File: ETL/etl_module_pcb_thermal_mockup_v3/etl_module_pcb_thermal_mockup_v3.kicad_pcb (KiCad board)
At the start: 4 copper layers, 44.1 x 57.5 mm, 23 parts, among them J3 Conn_02x05_Counter_Clockwise, U1 ETROC_dummy_thermal_sensors, U2 ETROC_dummy_thermal_sensors, U3 ETROC_dummy_thermal_sensors, U4 ETROC_dummy_thermal_sensors, U5 ADC088SO22, U6 ADC088SO22, U7 ADC088SO22, U8 ADC088SO22

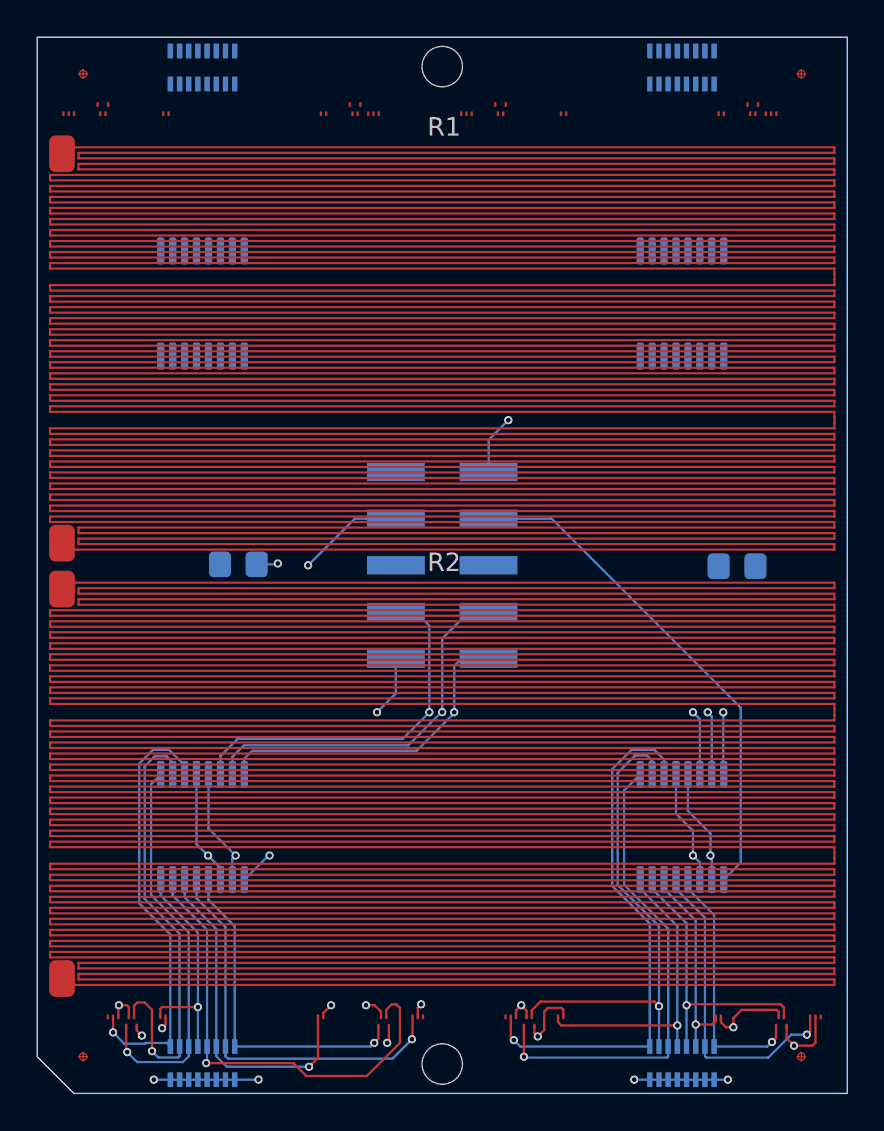
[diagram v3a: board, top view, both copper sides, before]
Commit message: Finishes redesigned draft of etl_module_pcb_thermal_mockup_v3
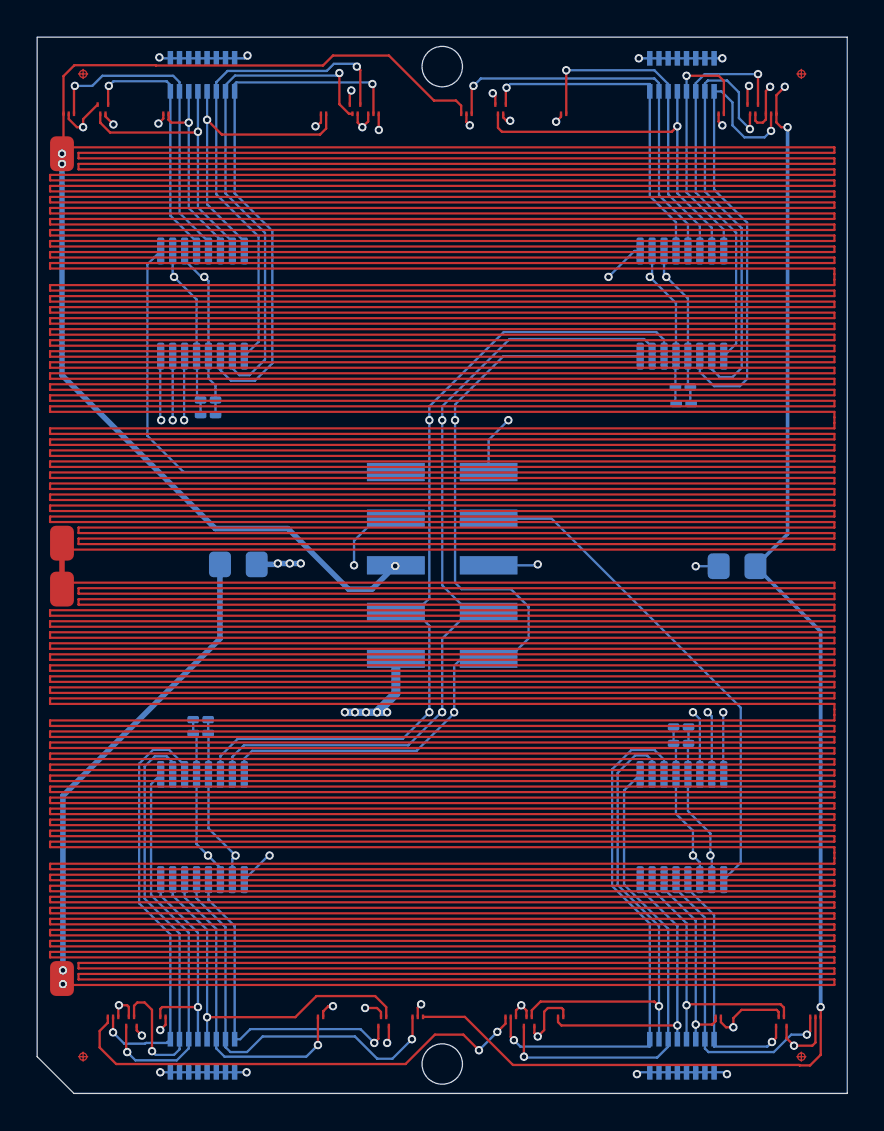
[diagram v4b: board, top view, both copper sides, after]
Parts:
- added C1: 1.0uF, Capacitor_SMD:C_0201_0603Metric_Pad0.64x0.40mm_HandSolder, B.Cu at (8.90, 37.1)
- added C2: 0.1uF, Capacitor_SMD:C_0201_0603Metric_Pad0.64x0.40mm_HandSolder, B.Cu at (8.90, 37.9)
- added C3: 1.0uF, Capacitor_SMD:C_0201_0603Metric_Pad0.64x0.40mm_HandSolder, B.Cu at (35.0, 37.5)
- added C4: 0.1uF, Capacitor_SMD:C_0201_0603Metric_Pad0.64x0.40mm_HandSolder, B.Cu at (35.0, 38.5)
- added C5: 1.0uF, Capacitor_SMD:C_0201_0603Metric_Pad0.64x0.40mm_HandSolder, B.Cu at (9.30, 20.6)
- added C6: 0.1uF, Capacitor_SMD:C_0201_0603Metric_Pad0.64x0.40mm_HandSolder, B.Cu at (9.30, 19.8)
- added C7: 1.0uF, Capacitor_SMD:C_0201_0603Metric_Pad0.64x0.40mm_HandSolder, B.Cu at (35.2, 19.9)
- added C8: 0.1uF, Capacitor_SMD:C_0201_0603Metric_Pad0.64x0.40mm_HandSolder, B.Cu at (35.1, 19.1)
- moved RN3 0.40 mm to (9.00, 2.05)
- moved RN4 0.40 mm to (35.1, 2.05)
- moved RN1 0.40 mm to (9.00, 55.5)
- moved RN2 0.40 mm to (35.1, 55.5)
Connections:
- R1 pad 1: Net-(R1-Pad1) -> VCC
- R1 pad 2: VCC -> Net-(R1-Pad2)
- R2 pad 1: Net-(JMPR1-Pad1) -> Net-(R1-Pad2)
- R2 pad 2: Net-(R1-Pad1) -> Net-(JMPR1-Pad1)
- RN3 pad 10: /X3EBR -> Net-(RN3-Pad10)
- RN3 pad 11: /X3LTR -> Net-(RN3-Pad11)
- RN3 pad 12: /X3ETR -> Net-(RN3-Pad12)
- RN3 pad 13: /X3LTL -> Net-(RN3-Pad13)
- RN3 pad 14: /X3ETL -> Net-(U3-Pad81)
- RN3 pad 15: /X3LBL -> Net-(U3-Pad117)
- RN3 pad 16: /X3EBL -> Net-(RN3-Pad16)
- RN3 pad 9: /X3LBR -> Net-(RN3-Pad9)
- RN4 pad 10: /X4EBR -> Net-(RN4-Pad10)
- RN4 pad 11: /X4LTR -> Net-(RN4-Pad11)
- RN4 pad 12: /X4ETR -> Net-(RN4-Pad12)
- RN4 pad 13: /X4LTL -> Net-(RN4-Pad13)
- RN4 pad 14: /X4ETL -> Net-(RN4-Pad14)
- RN4 pad 15: /X4LBL -> Net-(RN4-Pad15)
- RN4 pad 16: /X4EBL -> Net-(RN4-Pad16)
- RN4 pad 9: /X4LBR -> Net-(RN4-Pad9)
- U3 pad 1: VCC -> /VSS
- U3 pad 104: /X3LBR -> Net-(RN3-Pad16)
- U3 pad 107: /X3ETR -> Net-(RN3-Pad13)
- U3 pad 11: /X3LBL -> Net-(RN3-Pad10)
- U3 pad 117: /X3EBR -> Net-(U3-Pad117)
- U3 pad 121: /VSS -> VCC
- U3 pad 21: /X3LTL -> Net-(RN3-Pad12)
- U3 pad 3: /X3EBL -> Net-(RN3-Pad9)
- U3 pad 8: /X3ETL -> Net-(RN3-Pad11)
- U3 pad 81: /X3LTR -> Net-(U3-Pad81)
- U4 pad 1: VCC -> /VSS
- U4 pad 104: /X4LBR -> Net-(RN4-Pad16)
- U4 pad 107: /X4ETR -> Net-(RN4-Pad13)
- U4 pad 11: /X4LBL -> Net-(RN4-Pad10)
- U4 pad 117: /X4EBR -> Net-(RN4-Pad15)
- U4 pad 121: /VSS -> VCC
- U4 pad 21: /X4LTL -> Net-(RN4-Pad12)
- U4 pad 3: /X4EBL -> Net-(RN4-Pad9)
- U4 pad 8: /X4ETL -> Net-(RN4-Pad11)
- U4 pad 81: /X4LTR -> Net-(RN4-Pad14)
- U7 pad 10: /X3EBR -> Net-(RN3-Pad10)
- U7 pad 11: /X3LBR -> Net-(RN3-Pad9)
- U7 pad 4: /X3EBL -> Net-(RN3-Pad16)
- U7 pad 5: /X3LBL -> Net-(U3-Pad117)
- U7 pad 6: /X3ETL -> Net-(U3-Pad81)
- U7 pad 7: /X3LTL -> Net-(RN3-Pad13)
- U7 pad 8: /X3ETR -> Net-(RN3-Pad12)
- U7 pad 9: /X3LTR -> Net-(RN3-Pad11)
- U8 pad 10: /X4EBR -> Net-(RN4-Pad10)
- U8 pad 11: /X4LBR -> Net-(RN4-Pad9)
- U8 pad 4: /X4EBL -> Net-(RN4-Pad16)
- U8 pad 5: /X4LBL -> Net-(RN4-Pad15)
- U8 pad 6: /X4ETL -> Net-(RN4-Pad14)
- U8 pad 7: /X4LTL -> Net-(RN4-Pad13)
- U8 pad 8: /X4ETR -> Net-(RN4-Pad12)
- U8 pad 9: /X4LTR -> Net-(RN4-Pad11)
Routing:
- net VCC: track 0.00 -> 118.1 mm, vias 0 -> 5
- net /VSS: track 0.00 -> 102.5 mm, vias 0 -> 4
- net /CLK: track 36.9 -> 88.4 mm, vias 2 -> 4
- net /DOUT: track 39.6 -> 85.0 mm, vias 2 -> 4
- net /DIN: track 39.3 -> 84.6 mm, vias 2 -> 4
- net GND: track 37.5 -> 81.8 mm, vias 15 -> 37
- net +5V: track 23.5 -> 58.6 mm, vias 6 -> 13
- net Net-(RN3-Pad9): track 0.00 -> 29.5 mm, vias 0 -> 1
- net Net-(RN3-Pad10): track 0.00 -> 27.9 mm, vias 0 -> 1
- net Net-(JMPR1-Pad1): track 0.00 -> 26.7 mm, vias 0 -> 2
- net Net-(RN3-Pad11): track 0.00 -> 26.5 mm, vias 0 -> 1
- net Net-(RN4-Pad9): track 0.00 -> 26.3 mm, vias 0 -> 1
- net /CS3: track 0.00 -> 24.7 mm
- net Net-(RN4-Pad10): track 0.00 -> 24.3 mm, vias 0 -> 1
- net Net-(RN4-Pad15): track 0.00 -> 21.7 mm, vias 0 -> 1
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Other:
- board text added: "CS4 CS3 CS2 CS1 +5V VCC DOUT DIN CLK GND"
- board text added: "Pop JMPR1 for PCB heating Pop JMPR2 for chip heating"

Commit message: Work on etl_module_pcb_thermal_mockup_v3
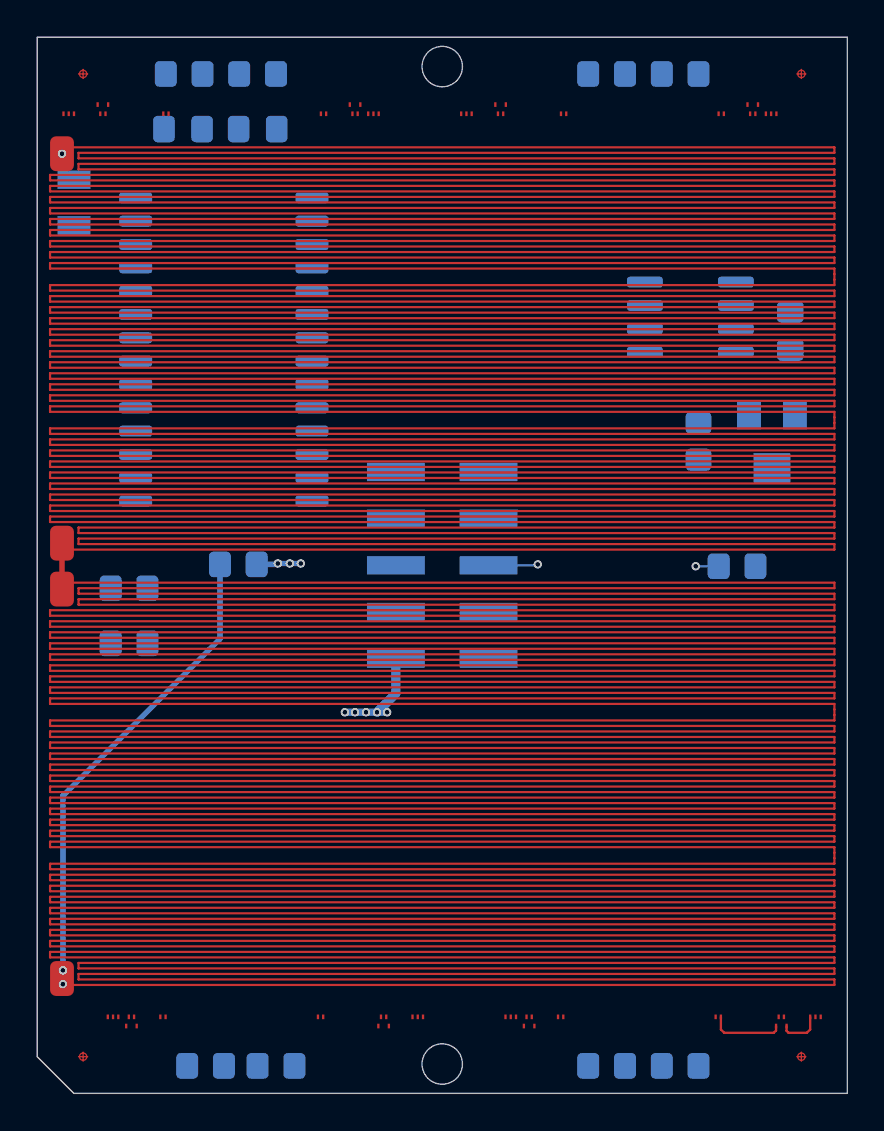
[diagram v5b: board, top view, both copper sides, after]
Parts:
- removed C4, C6, C8: 0.1uF, Capacitor_SMD:C_0201_0603Metric_Pad0.64x0.40mm_HandSolder
- removed C5, C7: 1.0uF, Capacitor_SMD:C_0201_0603Metric_Pad0.64x0.40mm_HandSolder
- removed RN1, RN2, RN3, RN4: 10k, Resistor_SMD:R_Array_Convex_8x0602
- removed U7, U8: ADC088SO22, Package_SO:TSSOP-16_4.4x5mm_P0.65mm
- added R10: 40k, Resistor_SMD:R_0805_2012Metric_Pad1.20x1.40mm_HandSolder, B.Cu at (12.0, 2.00)
- added R11: 40k, Resistor_SMD:R_0805_2012Metric_Pad1.20x1.40mm_HandSolder, B.Cu at (35.0, 2.00)
- added R12: 40k, Resistor_SMD:R_0805_2012Metric_Pad1.20x1.40mm_HandSolder, B.Cu at (31.0, 2.00)
- added R13: 1M, Resistor_SMD:R_0805_2012Metric_Pad1.20x1.40mm_HandSolder, B.Cu at (36.0, 22.0)
- added R3: 40k, Resistor_SMD:R_0805_2012Metric_Pad1.20x1.40mm_HandSolder, B.Cu at (5.00, 33.0)
- added R4: 40k, Resistor_SMD:R_0805_2012Metric_Pad1.20x1.40mm_HandSolder, B.Cu at (5.00, 30.0)
- added R5: 40k, Resistor_SMD:R_0805_2012Metric_Pad1.20x1.40mm_HandSolder, B.Cu at (13.0, 56.0)
- added R6: 40k, Resistor_SMD:R_0805_2012Metric_Pad1.20x1.40mm_HandSolder, B.Cu at (9.16, 56.0)
- added R7: 40k, Resistor_SMD:R_0805_2012Metric_Pad1.20x1.40mm_HandSolder, B.Cu at (31.0, 56.0)
- added R8: 40k, Resistor_SMD:R_0805_2012Metric_Pad1.20x1.40mm_HandSolder, B.Cu at (35.0, 56.0)
- added R9: 40k, Resistor_SMD:R_0805_2012Metric_Pad1.20x1.40mm_HandSolder, B.Cu at (8.00, 2.00)
- added RV1: 25k, Potentiometer_SMD:Potentiometer_Bourns_3224W_Vertical, B.Cu at (40.0, 22.0)
- added Y1: 32kHz, Crystal:Crystal_SMD_3215-2Pin_3.2x1.5mm, B.Cu at (2.00, 9.00)
- C1: value 1.0uF -> 1uF; footprint Capacitor_SMD:C_0201_0603Metric_Pad0.64x0.40mm_HandSolder -> Capacitor_SMD:C_0805_2012Metric_Pad1.18x1.45mm_HandSolder
- C2: footprint Capacitor_SMD:C_0201_0603Metric_Pad0.64x0.40mm_HandSolder -> Capacitor_SMD:C_0805_2012Metric_Pad1.18x1.45mm_HandSolder
- C3: value 1.0uF -> 10 uF; footprint Capacitor_SMD:C_0201_0603Metric_Pad0.64x0.40mm_HandSolder -> Capacitor_SMD:C_0805_2012Metric_Pad1.18x1.45mm_HandSolder
- U5: value ADC088SO22 -> AD77x8; footprint Package_SO:TSSOP-16_4.4x5mm_P0.65mm -> Package_SO:SOIC-28W_7.5x18.7mm_P1.27mm
- U6: value ADC088SO22 -> AD780; footprint Package_SO:TSSOP-16_4.4x5mm_P0.65mm -> Package_SO:SOIC-8_3.9x4.9mm_P1.27mm
- moved C3 39.9 mm to (12.0, 5.00)
- moved C1 38.4 mm to (41.0, 16.0), turned to -90 degrees
- moved C2 32.9 mm to (7.94, 5.00)
- moved U6 27.8 mm to (35.6, 15.2), turned to 180 degrees
- moved U5 26.0 mm to (10.2, 17.0), turned to 180 degrees
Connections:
- J3 pad 1: /CS4 -> /CS
- J3 pad 2: /CS3 -> /~{RESET}
- J3 pad 3: /CS2 -> /~{RDY}
- J3 pad 4: /CS1 -> unconnected-(J3-Pad4)
- U1 pad 104: Net-(RN1-Pad16) -> Net-(U1-Pad104)
- U1 pad 105: GND -> /LGAD1
- U1 pad 107: Net-(RN1-Pad13) -> Net-(U1-Pad107)
- U1 pad 108: GND -> Net-(U1-Pad108)
- U1 pad 11: Net-(RN1-Pad10) -> GND
- U1 pad 117: Net-(RN1-Pad15) -> Net-(U1-Pad108)
- U1 pad 119: GND -> /ETROC1
- U1 pad 12: GND -> Net-(U1-Pad12)
- U1 pad 21: Net-(RN1-Pad12) -> Net-(U1-Pad12)
- U1 pad 23: GND -> Net-(U1-Pad23)
- U1 pad 3: Net-(RN1-Pad9) -> GND
- U1 pad 5: GND -> Net-(U1-Pad5)
- U1 pad 8: Net-(RN1-Pad11) -> Net-(U1-Pad5)
- U1 pad 81: Net-(RN1-Pad14) -> Net-(U1-Pad23)
- U1 pad 83: GND -> Net-(U1-Pad104)
- U1 pad 9: GND -> Net-(U1-Pad107)
- U2 pad 104: Net-(RN2-Pad16) -> /LGAD2
- U2 pad 105: GND -> Net-(U2-Pad105)
- U2 pad 107: Net-(RN2-Pad13) -> Net-(U2-Pad107)
- U2 pad 108: GND -> /ETROC2
- U2 pad 11: Net-(RN2-Pad10) -> GND
- U2 pad 117: Net-(RN2-Pad15) -> /ETROC2
- U2 pad 119: GND -> Net-(U2-Pad119)
- U2 pad 12: GND -> Net-(U2-Pad12)
- U2 pad 21: Net-(RN2-Pad12) -> Net-(U2-Pad12)
- U2 pad 23: GND -> Net-(U2-Pad23)
- U2 pad 3: Net-(RN2-Pad9) -> GND
- U2 pad 5: GND -> Net-(U2-Pad5)
- U2 pad 8: Net-(RN2-Pad11) -> Net-(U2-Pad5)
- U2 pad 81: Net-(RN2-Pad14) -> Net-(U2-Pad23)
- U2 pad 83: GND -> /LGAD2
- U2 pad 9: GND -> Net-(U2-Pad107)
- U3 pad 1: /VSS -> VCC
- U3 pad 104: Net-(RN3-Pad16) -> /LGAD3
- U3 pad 105: GND -> Net-(U3-Pad105)
- U3 pad 107: Net-(RN3-Pad13) -> Net-(U3-Pad107)
- U3 pad 108: GND -> /ETROC3
- U3 pad 11: Net-(RN3-Pad10) -> GND
- U3 pad 117: Net-(U3-Pad117) -> /ETROC3
- U3 pad 119: GND -> Net-(U3-Pad119)
- U3 pad 12: GND -> Net-(U3-Pad12)
- U3 pad 121: VCC -> /VSS
- U3 pad 21: Net-(RN3-Pad12) -> Net-(U3-Pad12)
- U3 pad 23: GND -> Net-(U3-Pad23)
- U3 pad 3: Net-(RN3-Pad9) -> GND
- U3 pad 5: GND -> Net-(U3-Pad5)
- U3 pad 8: Net-(RN3-Pad11) -> Net-(U3-Pad5)
- U3 pad 81: Net-(U3-Pad81) -> Net-(U3-Pad23)
- U3 pad 83: GND -> /LGAD3
- U3 pad 9: GND -> Net-(U3-Pad107)
- U4 pad 1: /VSS -> VCC
- U4 pad 104: Net-(RN4-Pad16) -> /LGAD4
- U4 pad 105: GND -> Net-(U4-Pad105)
- U4 pad 107: Net-(RN4-Pad13) -> Net-(U4-Pad107)
- U4 pad 108: GND -> /ETROC4
- U4 pad 11: Net-(RN4-Pad10) -> GND
- U4 pad 117: Net-(RN4-Pad15) -> /ETROC4
- U4 pad 119: GND -> Net-(U4-Pad119)
- U4 pad 12: GND -> Net-(U4-Pad12)
- U4 pad 121: VCC -> /VSS
- U4 pad 21: Net-(RN4-Pad12) -> Net-(U4-Pad12)
- U4 pad 23: GND -> Net-(U4-Pad23)
- U4 pad 3: Net-(RN4-Pad9) -> GND
- U4 pad 5: GND -> Net-(U4-Pad5)
- U4 pad 8: Net-(RN4-Pad11) -> Net-(U4-Pad5)
- U4 pad 81: Net-(RN4-Pad14) -> Net-(U4-Pad23)
- U4 pad 83: GND -> /LGAD4
- U4 pad 9: GND -> Net-(U4-Pad107)
- U5 pad 1: /CS1 -> /ETROC4
- U5 pad 10: Net-(RN1-Pad10) -> /LGAD2
- U5 pad 11: Net-(RN1-Pad9) -> /ETROC3
- U5 pad 12: GND -> /V_{ref}
- U5 pad 13: +5V -> /2.5V
- U5 pad 14: /DIN -> GND
- U5 pad 15: /DOUT -> /LGAD3
- U5 pad 16: /CLK -> unconnected-(U5-Pad16)
- U5 pad 2: +5V -> /LGAD4
- U5 pad 3: GND -> +5V
- U5 pad 4: Net-(RN1-Pad16) -> GND
- U5 pad 5: Net-(RN1-Pad15) -> GND
- U5 pad 6: Net-(RN1-Pad14) -> /V_{ref}
- U5 pad 7: Net-(RN1-Pad13) -> /ETROC1
- U5 pad 8: Net-(RN1-Pad12) -> /LGAD1
- U5 pad 9: Net-(RN1-Pad11) -> /ETROC2
- U6 pad 1: /CS2 -> unconnected-(U6-Pad1)
- U6 pad 3: GND -> unconnected-(U6-Pad3)
- U6 pad 4: Net-(RN2-Pad16) -> GND
- U6 pad 5: Net-(RN2-Pad15) -> /2.5V
- U6 pad 6: Net-(RN2-Pad14) -> unconnected-(U6-Pad6)
- U6 pad 7: Net-(RN2-Pad13) -> unconnected-(U6-Pad7)
- U6 pad 8: Net-(RN2-Pad12) -> unconnected-(U6-Pad8)
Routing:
- net VCC: track 118.1 -> 0.00 mm, vias 5 -> 1
- net /VSS: track 102.5 -> 0.00 mm, vias 4 -> 0
- net /CLK: track 88.4 -> 0.00 mm, vias 4 -> 0
- net /DOUT: track 85.0 -> 0.00 mm, vias 4 -> 0
- net /DIN: track 84.6 -> 0.00 mm, vias 4 -> 0
- net GND: track 81.8 -> 9.32 mm, vias 37 -> 9
- net +5V: track 58.6 -> 2.70 mm, vias 13 -> 1
- net Net-(RN3-Pad9): track 29.5 -> 0.00 mm, vias 1 -> 0
- net Net-(RN2-Pad9): track 29.1 -> 0.00 mm, vias 1 -> 0
- net Net-(RN3-Pad10): track 27.9 -> 0.00 mm, vias 1 -> 0
- net /CS2: track 27.7 -> 0.00 mm
- net Net-(RN3-Pad11): track 26.5 -> 0.00 mm, vias 1 -> 0
- net Net-(RN4-Pad9): track 26.3 -> 0.00 mm, vias 1 -> 0
- net Net-(RN2-Pad10): track 26.2 -> 0.00 mm, vias 1 -> 0
- net Net-(RN2-Pad11): track 26.0 -> 0.00 mm, vias 1 -> 0
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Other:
- board text added: "CS ~{RST} ~{RDY} UNC +5V VCC DOUT DIN CLK GND"
- board text removed: "CS4 CS3 CS2 CS1 +5V VCC DOUT DIN CLK GND"

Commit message: Almost finished routing on etl_module_pcb_thermal_mockup_v3
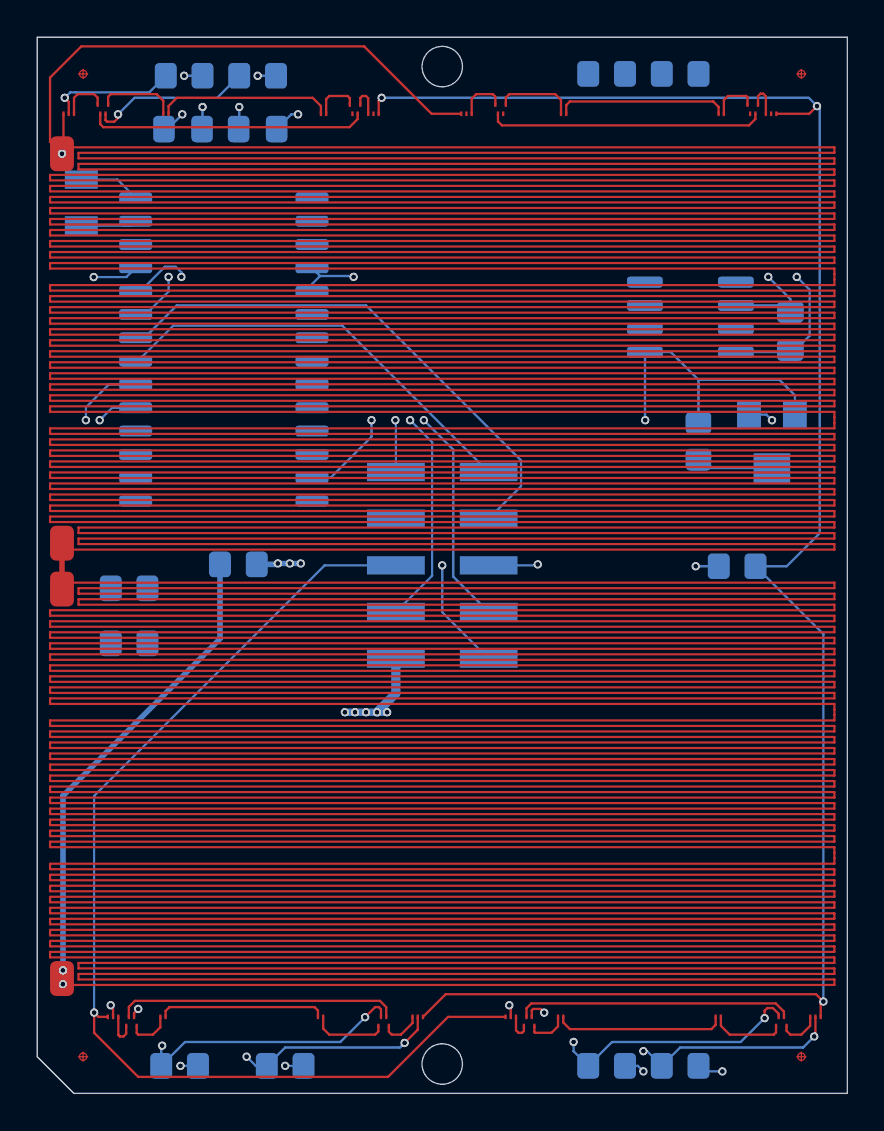
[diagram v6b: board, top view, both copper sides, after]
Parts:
- moved R5 5.25 mm to (7.75, 56.0)
- moved R6 4.34 mm to (13.5, 56.0)
- moved R10 4.00 mm to (8.00, 2.10)
- moved R9 4.00 mm to (12.0, 2.10)
- moved Y1 0.40 mm to (2.40, 9.00)
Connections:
- J3 pad 7: /DOUT -> /DIN
- J3 pad 8: /DIN -> /DOUT
- R10 pad 2: Net-(U3-Pad119) -> /ETROC3
- R11 pad 2: Net-(U4-Pad105) -> /LGAD4
- R12 pad 2: Net-(U4-Pad119) -> /ETROC4
- R7 pad 2: Net-(U2-Pad105) -> /LGAD2
- R8 pad 2: Net-(U2-Pad119) -> /ETROC2
- R9 pad 2: Net-(U3-Pad105) -> /LGAD3
- U2 pad 104: /LGAD2 -> Net-(U2-Pad83)
- U2 pad 105: Net-(U2-Pad105) -> /LGAD2
- U2 pad 108: /ETROC2 -> Net-(U2-Pad117)
- U2 pad 117: /ETROC2 -> Net-(U2-Pad117)
- U2 pad 119: Net-(U2-Pad119) -> /ETROC2
- U2 pad 83: /LGAD2 -> Net-(U2-Pad83)
- U3 pad 1: VCC -> /VSS
- U3 pad 104: /LGAD3 -> Net-(U3-Pad104)
- U3 pad 105: Net-(U3-Pad105) -> /LGAD3
- U3 pad 108: /ETROC3 -> Net-(U3-Pad108)
- U3 pad 117: /ETROC3 -> Net-(U3-Pad108)
- U3 pad 119: Net-(U3-Pad119) -> /ETROC3
- U3 pad 121: /VSS -> VCC
- U3 pad 83: /LGAD3 -> Net-(U3-Pad104)
- U4 pad 1: VCC -> /VSS
- U4 pad 104: /LGAD4 -> Net-(U4-Pad104)
- U4 pad 105: Net-(U4-Pad105) -> /LGAD4
- U4 pad 108: /ETROC4 -> Net-(U4-Pad108)
- U4 pad 117: /ETROC4 -> Net-(U4-Pad108)
- U4 pad 119: Net-(U4-Pad119) -> /ETROC4
- U4 pad 121: /VSS -> VCC
- U4 pad 83: /LGAD4 -> Net-(U4-Pad104)
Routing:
- net /VSS: track 0.00 -> 103.4 mm, vias 0 -> 3
- net VCC: track 0.00 -> 91.3 mm, vias 1 -> 2
- net /ETROC2: track 2.36 -> 62.4 mm, vias 0 -> 2
- net /LGAD2: track 4.06 -> 62.5 mm, vias 0 -> 2
- net /LGAD1: track 0.00 -> 48.6 mm, vias 0 -> 2
- net /ETROC1: track 0.00 -> 44.9 mm, vias 0 -> 2
- net /2.5V: track 0.00 -> 37.9 mm, vias 0 -> 2
- net /CLK: track 0.00 -> 33.3 mm, vias 0 -> 2
- net /DIN: track 0.00 -> 32.5 mm, vias 0 -> 2
- net /DOUT: track 0.00 -> 31.5 mm, vias 0 -> 2
- net /~{RDY}: track 0.00 -> 29.1 mm
- net /CS: track 0.00 -> 23.3 mm
- net /~{RESET}: track 0.00 -> 23.0 mm, vias 0 -> 2
- net GND: track 9.32 -> 29.9 mm, vias 9 -> 19
- net Net-(U1-Pad107): track 0.00 -> 15.4 mm
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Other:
- board text added: "CS ~{RST} ~{RDY} NC +5V VCC DOUT DIN CLK GND"
- board text added: "Populate JMPR1 for PCB heating Populate JMPR2 for chip heating"
- board text removed: "CS ~{RST} ~{RDY} UNC +5V VCC DOUT DIN CLK GND"
- board text removed: "Pop JMPR1 for PCB heating Pop JMPR2 for chip heating"
